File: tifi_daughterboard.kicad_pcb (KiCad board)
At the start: 2 copper layers, 57.4 x 32.3 mm, 19 parts, among them J1 SSW-110-23-F-D, J2 SSW-110-23-F-D, J3 SM04B-SRSS-TB(LF)(SN), J4 SSW-103-02-T-S-RA, Q1 BSS138LT1G, U1 SGP40-D-R4, U2 SHT40-AD1B-R3

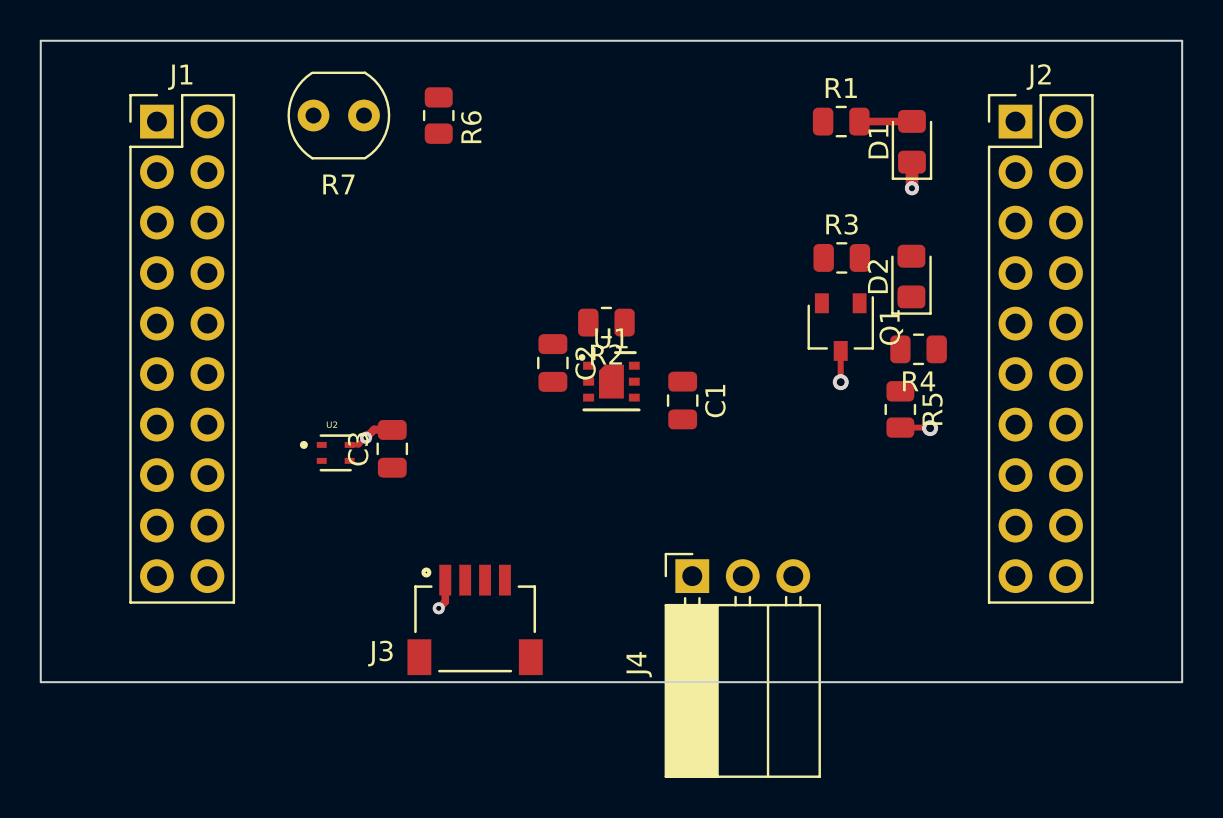
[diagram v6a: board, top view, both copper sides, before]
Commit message: Move VOC sensor closer to header.
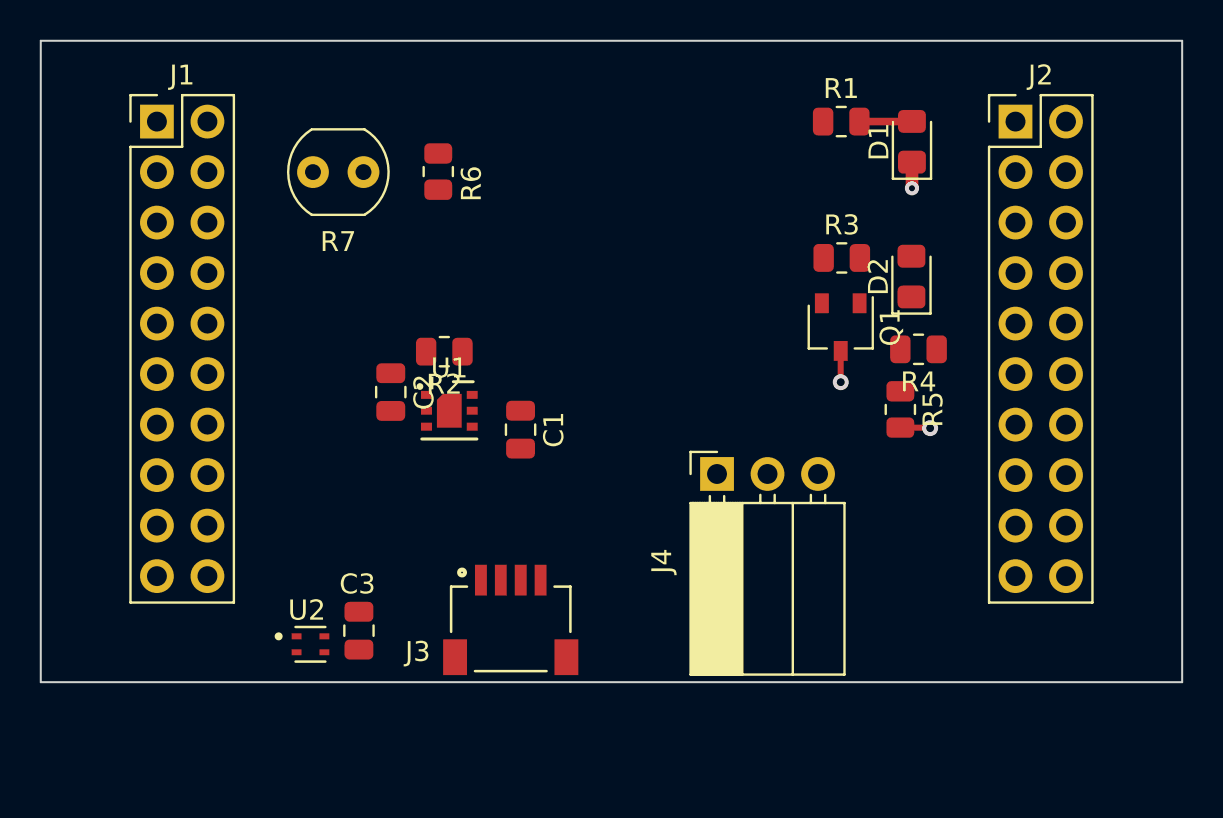
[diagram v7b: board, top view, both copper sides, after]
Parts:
- moved U2 9.71 mm to (129.6, 99.9)
- moved C3 9.30 mm to (132.1, 99.3)
- moved R2 8.28 mm to (136.4, 85.2)
- moved C1 8.28 mm to (140.2, 89.2)
- moved U1 8.28 mm to (136.6, 88.2)
- moved C2 8.28 mm to (133.7, 87.3)
- moved J4 5.29 mm to (150.1, 91.4)
- moved R7 2.84 mm to (132.3, 76.2)
- moved R6 2.82 mm to (136.1, 76.2)
- moved J3 1.79 mm to (139.7, 96.7)
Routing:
- net GND: track 8.41 -> 4.39 mm, vias 5 -> 3
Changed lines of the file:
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@@
   )
   (footprint "Resistor_SMD:R_0805_2012Metric" (layer "F.Cu")
-    (at 144.526 83.7692 180)
+    (at 136.3726 85.2322 180)
     (descr "Resistor SMD 0805 (2012 Metric), square (rectangular) end terminal, IPC_7351 nominal, (Body size source: IPC-SM-782 page 72, https://www.pcb-3d.com/wordpress/wp-content/uploads/ipc-sm-782a_amendment_1_and_2.pdf), generated with kicad-footprint-generator")
     (tags "resistor")
@@
   )
   (footprint "Capacitor_SMD:C_0805_2012Metric" (layer "F.Cu")
-    (at 141.8336 85.8012 -90)
+    (at 133.6802 87.2642 -90)
     (descr "Capacitor SMD 0805 (2012 Metric), square (rectangular) end terminal, IPC_7351 nominal, (Body size source: IPC-SM-782 page 76, https://www.pcb-3d.com/wordpress/wp-content/uploads/ipc-sm-782a_amendment_1_and_2.pdf, https://docs.google.com/spreadsheets/d/1BsfQQcO9C6DZCsRaXUlFlo91Tg2WpOkGARC1WS5S8t0/edit?usp=sharing), generated with kicad-footprint-generator")
     (tags "capacitor")
@@
   )
   (footprint "OptoDevice:R_LDR_4.9x4.2mm_P2.54mm_Vertical" (layer "F.Cu")
-    (at 132.334 73.3552 180)
+    (at 132.3086 76.2 180)
     (descr "Resistor, LDR 4.9x4.2mm")
     (tags "Resistor LDR4.9x4.2")
@@
   )
   (footprint "Capacitor_SMD:C_0805_2012Metric" (layer "F.Cu")
-    (at 133.7564 90.1192 90)
+    (at 132.08 99.2632 90)
     (descr "Capacitor SMD 0805 (2012 Metric), square (rectangular) end terminal, IPC_7351 nominal, (Body size source: IPC-SM-782 page 76, https://www.pcb-3d.com/wordpress/wp-content/uploads/ipc-sm-782a_amendment_1_and_2.pdf, https://docs.google.com/spreadsheets/d/1BsfQQcO9C6DZCsRaXUlFlo91Tg2WpOkGARC1WS5S8t0/edit?usp=sharing), generated with kicad-footprint-generator")
     (tags "capacitor")
@@
     (property "Sheetname" "")
     (attr smd)
-    (fp_text reference "C3" (at 0 -1.68 90) (layer "F.SilkS")
+    (fp_text reference "C3" (at 2.3368 -0.0762 180) (layer "F.SilkS")
       (effects (font (size 1 1) (thickness 0.15)))
     )
@@
   )
   (footprint "Connector_PinSocket_2.54mm:PinSocket_1x03_P2.54mm_Horizontal" (layer "F.Cu")
-    (at 148.844 96.52 90)
+    (at 150.0886 91.3834 90)
     (descr "Through hole angled socket strip, 1x03, 2.54mm pitch, 8.51mm socket length, single row (from Kicad 4.0.7), script generated")
     (tags "Through hole angled socket strip THT 1x03 2.54mm single row")
@@
   )
   (footprint "TiFi Footprints:DFN-6-1EP_2.44x2.44mm_P0.8mm_EP1.25x1.7mm" (layer "F.Cu")
-    (at 144.78 86.741)
+    (at 136.6266 88.204)
     (descr "DC6 Package; 6-Lead Plastic DFN (2mm x 2mm) (see Linear Technology DFN_6_05-08-1703.pdf)")
     (tags "DFN 0.5")
@@
   )
   (footprint "Resistor_SMD:R_0805_2012Metric" (layer "F.Cu")
-    (at 136.0932 73.3552 -90)
+    (at 136.0678 76.1746 -90)
     (descr "Resistor SMD 0805 (2012 Metric), square (rectangular) end terminal, IPC_7351 nominal, (Body size source: IPC-SM-782 page 72, https://www.pcb-3d.com/wordpress/wp-content/uploads/ipc-sm-782a_amendment_1_and_2.pdf), generated with kicad-footprint-generator")
     (tags "resistor")
@@
   )
   (footprint "STEMMA_QT:JST_SM04B-SRSS-TB(LF)(SN)" (layer "F.Cu")
-    (at 137.922 96.7232)
+    (at 139.715 96.7232)
     (property "Sheetfile" "tifi_daughterboard.kicad_sch")
     (property "Sheetname" "")
@@
   )
   (footprint "Capacitor_SMD:C_0805_2012Metric" (layer "F.Cu")
-    (at 148.3614 87.691 -90)
+    (at 140.208 89.154 -90)
     (descr "Capacitor SMD 0805 (2012 Metric), square (rectangular) end terminal, IPC_7351 nominal, (Body size source: IPC-SM-782 page 76, https://www.pcb-3d.com/wordpress/wp-content/uploads/ipc-sm-782a_amendment_1_and_2.pdf, https://docs.google.com/spreadsheets/d/1BsfQQcO9C6DZCsRaXUlFlo91Tg2WpOkGARC1WS5S8t0/edit?usp=sharing), generated with kicad-footprint-generator")
     (tags "capacitor")
@@
   )
   (footprint "SHT40:XDCR_SHT40-AD1B-R2" (layer "F.Cu")
-    (at 130.9116 90.3224)
+    (at 129.6416 99.949)
     (property "Sheetfile" "tifi_daughterboard.kicad_sch")
     (property "Sheetname" "")
     (attr through_hole)
-    (fp_text reference "U2" (at -0.184 -1.4032) (layer "F.SilkS")
-      (effects (font (size 0.32 0.32) (thickness 0.15)))
+    (fp_text reference "U2" (at -0.184 -1.708) (layer "F.SilkS")
+      (effects (font (size 1.016 1.016) (thickness 0.15)))
     )
     (fp_text value "SHT40-AD1B-R3" (at 2.4576 1.4032) (layer "F.Fab")
@@
       (polygon
         (pts
-          (xy 130.1616 89.5724)
-          (xy 131.6616 89.5724)
-          (xy 131.6616 89.7724)
-          (xy 131.3616 89.7724)
-          (xy 131.3616 90.0724)
-          (xy 131.6616 90.0724)
-          (xy 131.6616 90.5724)
-          (xy 131.3616 90.5724)
-          (xy 131.3616 90.8724)
-          (xy 131.6616 90.8724)
-          (xy 131.6616 91.0724)
-          (xy 130.1616 91.0724)
-          (xy 130.1616 90.8724)
-          (xy 130.4616 90.8724)
-          (xy 130.4616 90.5724)
-          (xy 130.1616 90.5724)
-          (xy 130.1616 90.0724)
-          (xy 130.4616 90.0724)
-          (xy 130.4616 89.7724)
-          (xy 130.1616 89.7724)
+          (xy 128.8916 99.199)
+          (xy 130.3916 99.199)
+          (xy 130.3916 99.399)
+          (xy 130.0916 99.399)
+          (xy 130.0916 99.699)
+          (xy 130.3916 99.699)
+          (xy 130.3916 100.199)
+          (xy 130.0916 100.199)
+          (xy 130.0916 100.499)
+          (xy 130.3916 100.499)
+          (xy 130.3916 100.699)
+          (xy 128.8916 100.699)
+          (xy 128.8916 100.499)
+          (xy 129.1916 100.499)
+          (xy 129.1916 100.199)
+          (xy 128.8916 100.199)
+          (xy 128.8916 99.699)
+          (xy 129.1916 99.699)
+          (xy 129.1916 99.399)
+          (xy 128.8916 99.399)
         )
       )
@@
       (polygon
         (pts
-          (xy 130.1616 89.5724)
-          (xy 131.6616 89.5724)
-          (xy 131.6616 89.7724)
-          (xy 131.3616 89.7724)
-          (xy 131.3616 90.0724)
-          (xy 131.6616 90.0724)
-          (xy 131.6616 90.5724)
-          (xy 131.3616 90.5724)
-          (xy 131.3616 90.8724)
-          (xy 131.6616 90.8724)
-          (xy 131.6616 91.0724)
-          (xy 130.1616 91.0724)
-          (xy 130.1616 90.8724)
-          (xy 130.4616 90.8724)
-          (xy 130.4616 90.5724)
-          (xy 130.1616 90.5724)
-          (xy 130.1616 90.0724)
-          (xy 130.4616 90.0724)
-          (xy 130.4616 89.7724)
-          (xy 130.1616 89.7724)
+          (xy 128.8916 99.199)
+          (xy 130.3916 99.199)
+          (xy 130.3916 99.399)
+          (xy 130.0916 99.399)
+          (xy 130.0916 99.699)
+          (xy 130.3916 99.699)
+          (xy 130.3916 100.199)
+          (xy 130.0916 100.199)
+          (xy 130.0916 100.499)
+          (xy 130.3916 100.499)
+          (xy 130.3916 100.699)
+          (xy 128.8916 100.699)
+          (xy 128.8916 100.499)
+          (xy 129.1916 100.499)
+          (xy 129.1916 100.199)
+          (xy 128.8916 100.199)
+          (xy 128.8916 99.699)
+          (xy 129.1916 99.699)
+          (xy 129.1916 99.399)
+          (xy 128.8916 99.399)
         )
       )
@@
   )
   (gr_rect (start 116.078 69.596) (end 173.482 101.854) (layer "Edge.Cuts") (width 0.1016) (fill none))
-  (segment (start 131.6116 89.9224) (end 132.0736 89.9224) (width 0.254) (layer "F.Cu") (net 2))
   (segment (start 159.893 77.0128) (end 159.893 75.701) (width 0.635) (layer "F.Cu") (net 2))
   (segment (start 159.3088 89.0505) (end 160.7801 89.0505) (width 0.3048) (layer "F.Cu") (net 2))
-  (segment (start 133.7412 89.154) (end 133.7564 89.1692) (width 0.4064) (layer "F.Cu") (net 2))
-  (segment (start 132.4356 89.5604) (end 132.842 89.154) (width 0.4064) (layer "F.Cu") (net 2))
-  (segment (start 136.422 97.8102) (end 136.422 96.7232) (width 0.381) (layer "F.Cu") (net 2))
   (segment (start 156.3116 85.1959) (end 156.3116 86.7664) (width 0.3048) (layer "F.Cu") (net 2))
-  (segment (start 132.0736 89.9224) (end 132.4356 89.5604) (width 0.254) (layer "F.Cu") (net 2))
-  (segment (start 132.842 89.154) (end 133.7412 89.154) (width 0.4064) (layer "F.Cu") (net 2))
-  (segment (start 136.0932 98.139) (end 136.422 97.8102) (width 0.381) (layer "F.Cu") (net 2))
   (segment (start 160.7801 89.0505) (end 160.8074 89.0778) (width 0.3048) (layer "F.Cu") (net 2))
   (via (at 160.8074 89.0778) (size 0.8) (drill 0.4) (layers "F.Cu" "B.Cu") (net 2))
-  (via (at 132.4356 89.5604) (size 0.6096) (drill 0.254) (layers "F.Cu" "B.Cu") (free) (net 2))
-  (via (at 136.0932 98.139) (size 0.6096) (drill 0.254) (layers "F.Cu" "B.Cu") (free) (net 2))
   (via (at 159.893 77.0128) (size 0.7112) (drill 0.3048) (layers "F.Cu" "B.Cu") (free) (net 2))
   (via (at 156.3116 86.7664) (size 0.8) (drill 0.4) (layers "F.Cu" "B.Cu") (net 2))
   (segment (start 157.2495 73.66) (end 159.884 73.66) (width 0.381) (layer "F.Cu") (net 3))
   (segment (start 159.884 73.66) (end 159.893 73.651) (width 0.381) (layer "F.Cu") (net 3))
-  (segment (start 143.5119 83.8708) (end 143.7151 84.074) (width 0.508) (layer "F.Cu") (net 43))
+  (segment (start 135.3585 85.3338) (end 135.5617 85.537) (width 0.508) (layer "F.Cu") (net 43))
 )
